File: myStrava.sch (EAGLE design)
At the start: 53 parts, among them Y1 16MHz

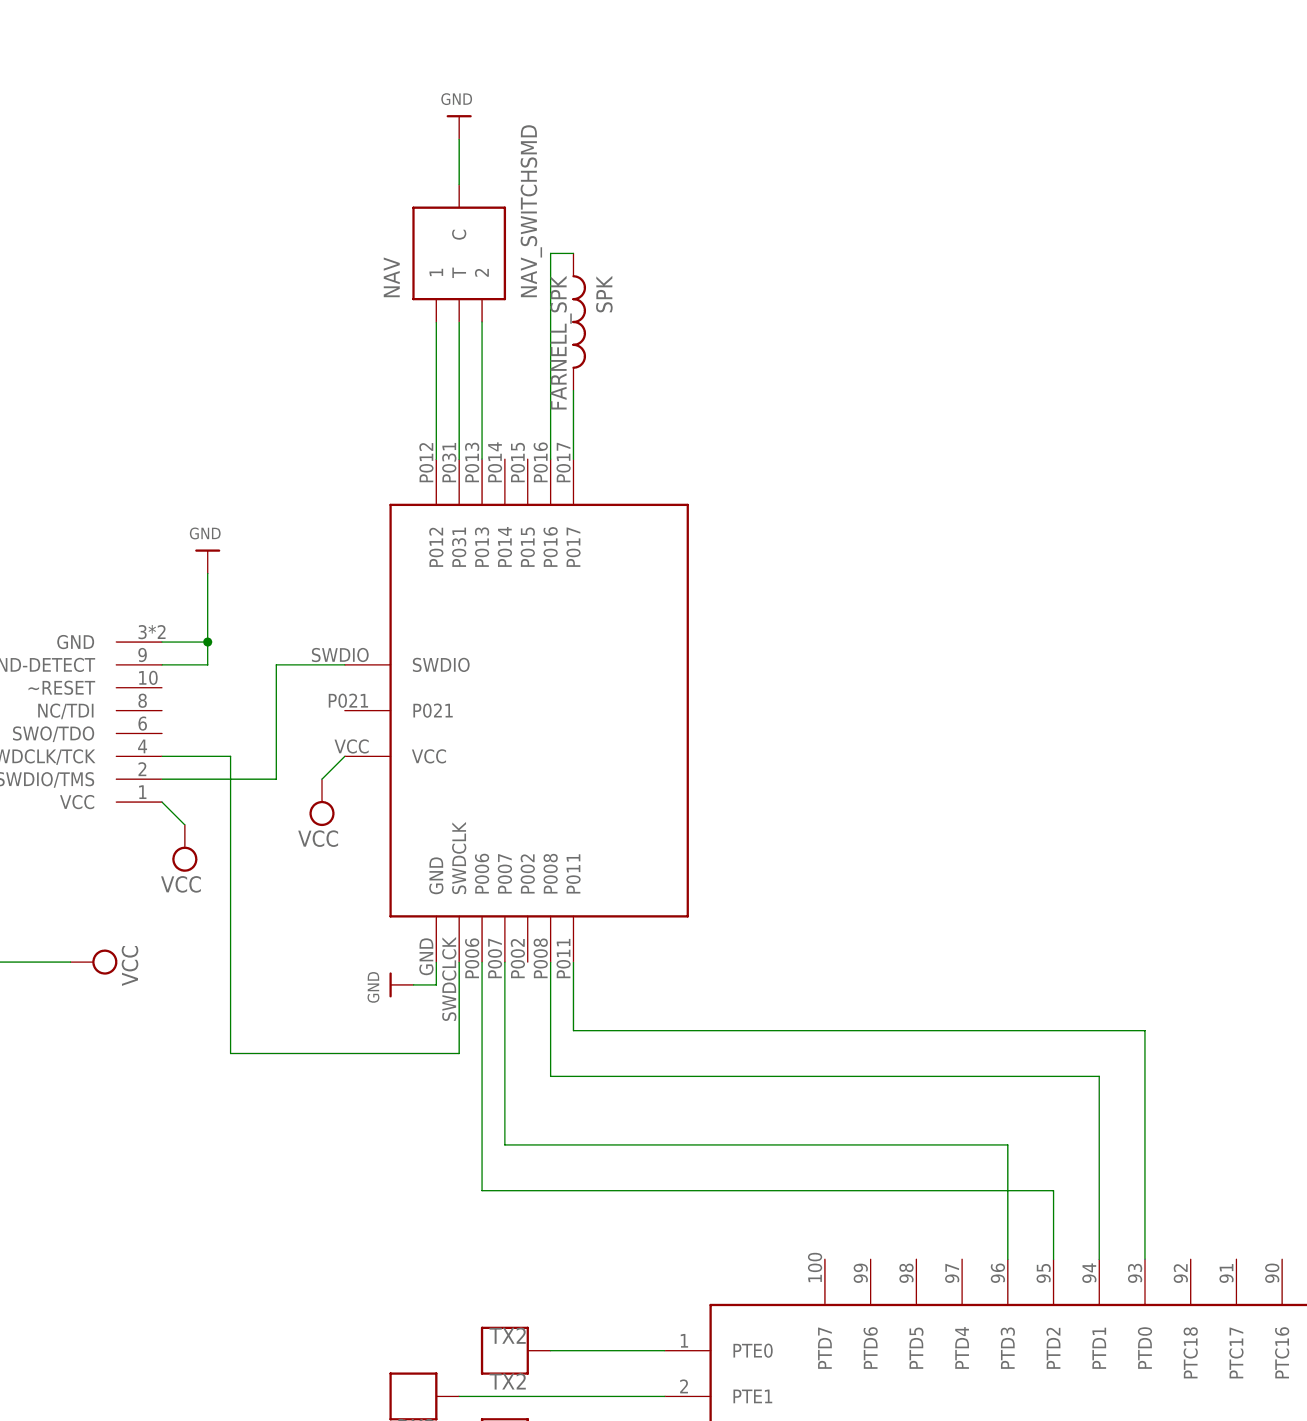
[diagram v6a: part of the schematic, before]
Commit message: Ajout du M8 en face inferieure
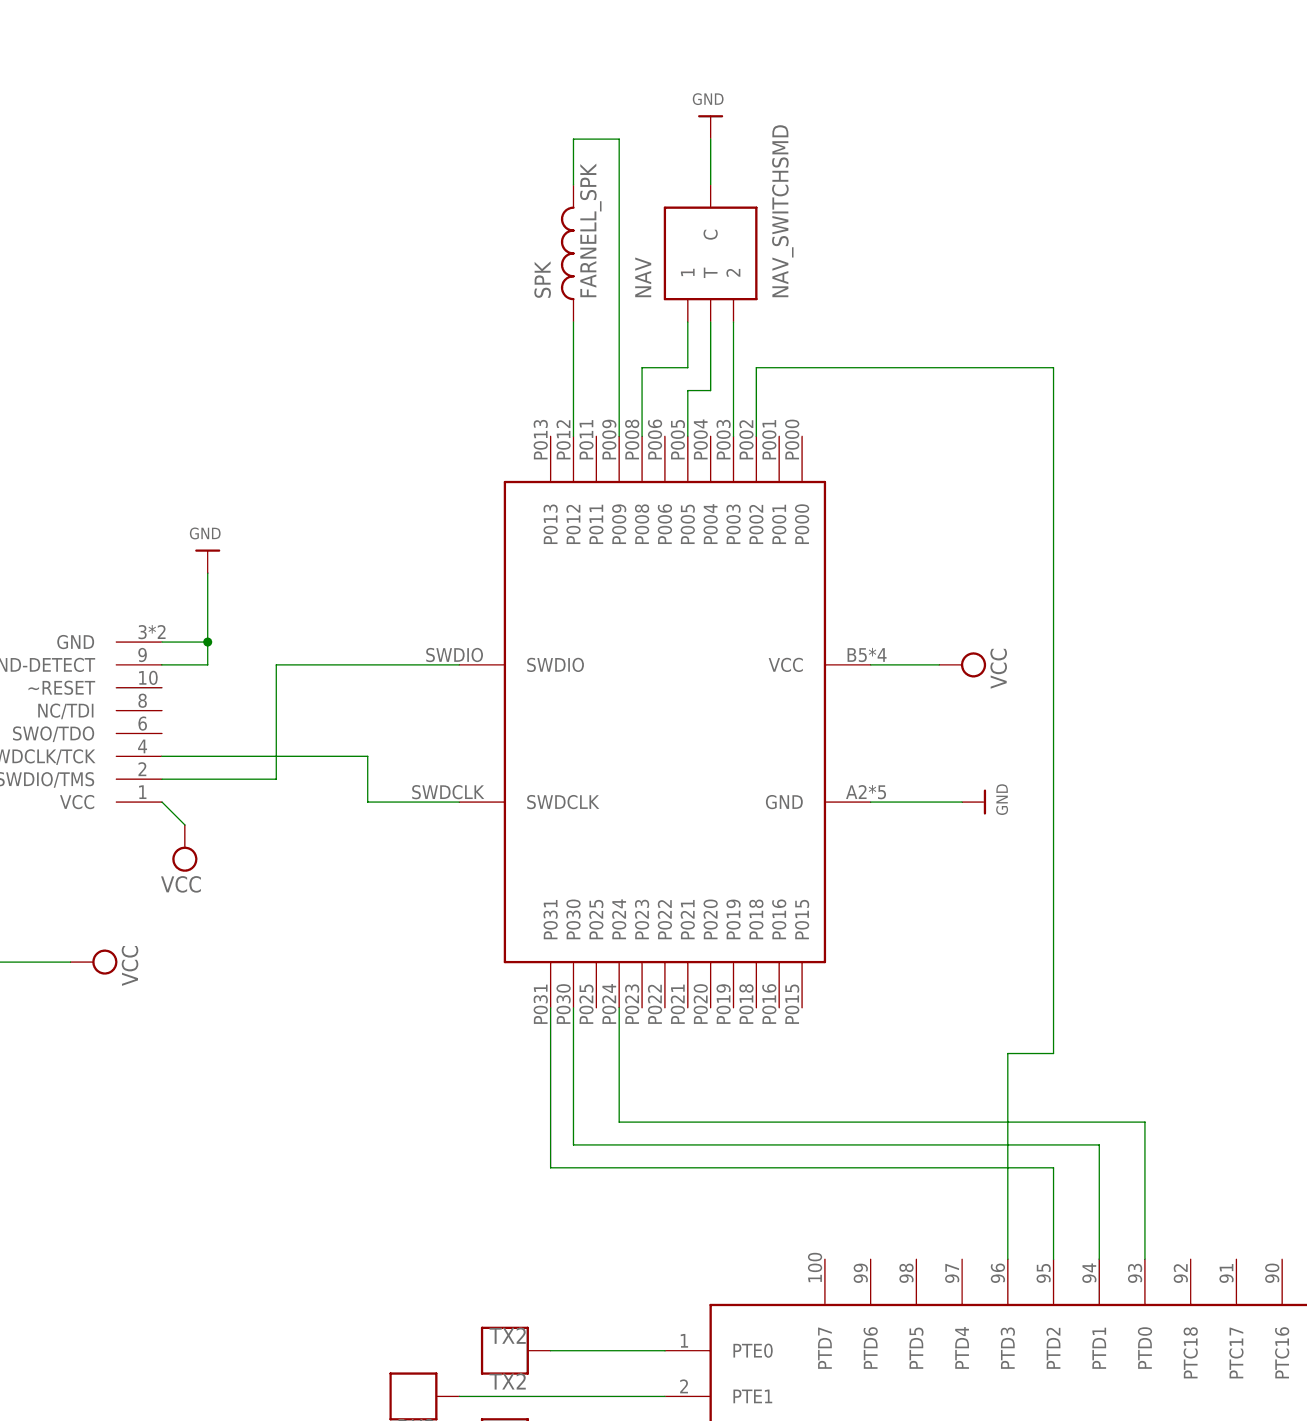
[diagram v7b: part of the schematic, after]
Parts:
- D52Q: value ANTAP28 -> N548; device D52Q:ANTAP28 -> N548:N548
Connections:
- removed net MK_RX3: D52Q.P006, MK20DN512.PTD2
- removed net MK_TX3: D52Q.P007, MK20DN512.PTD3
- new net N$13: D52Q.P024, MK20DN512.PTD0
- new net N$29: D52Q.P002, MK20DN512.PTD3
- net N$10: now also D52Q.P003; no longer D52Q.P013
- net N$18: now also D52Q.P030; no longer D52Q.P008
- net N$21: now also D52Q.P031, MK20DN512.PTD2; no longer D52Q.P011, MK20DN512.PTD0
- net N$3: now also D52Q.P012, SPK.1; no longer D52Q.P017, SPK.2
- net N$7: now also D52Q.P009, SPK.2; no longer D52Q.P016, SPK.1
- net N$8: now also D52Q.P008; no longer D52Q.P012
- net N$9: now also D52Q.P005; no longer D52Q.P031
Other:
- moved on the sheet: NAV, SPK

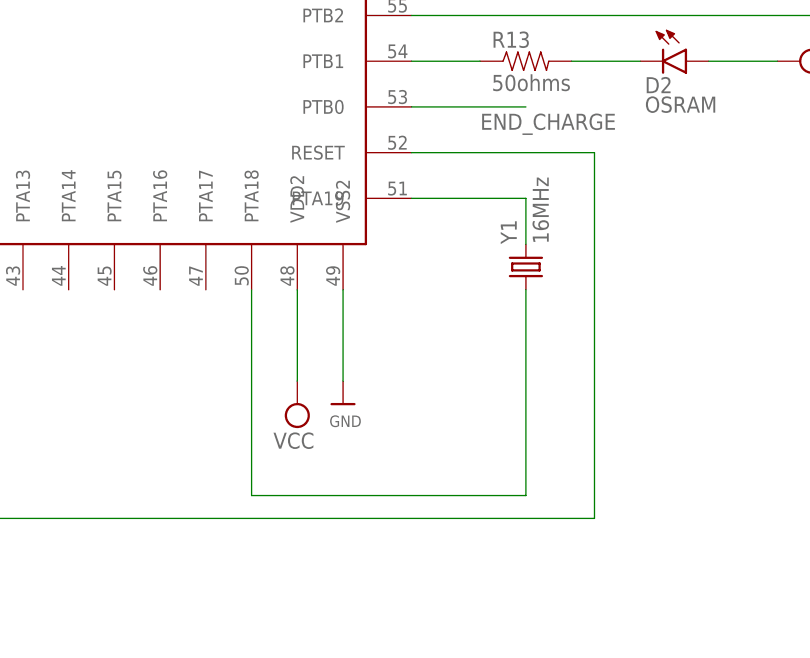
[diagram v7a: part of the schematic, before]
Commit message: Modif d'une via
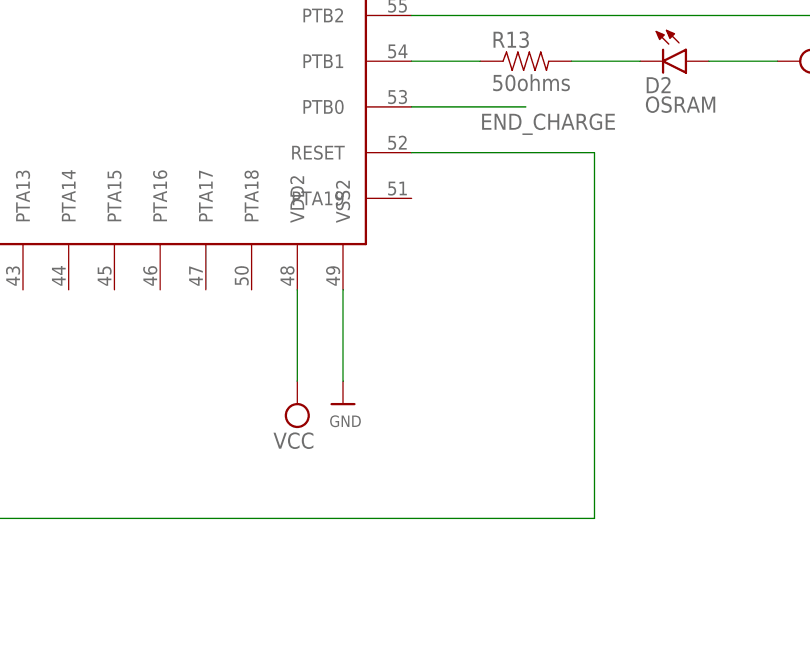
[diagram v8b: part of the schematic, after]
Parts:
- removed Y1: 16MHz, SparkFun-FreqCtrl:CRYSTALHC49UV
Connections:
- removed net N$14: MK20DN512.PTA19, Y1.2
- removed net N$19: MK20DN512.PTA18, Y1.1
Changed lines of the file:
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@@
 <part name="SUPPLY14" library="supply2" deviceset="VCC" device=""/>
 <part name="U$27" library="microbuilder" deviceset="GND" device=""/>
-<part name="Y1" library="SparkFun-FreqCtrl" deviceset="CRYSTAL" device="HC49UV" value="16MHz"/>
 <part name="SUPPLY15" library="supply2" deviceset="VCC" device=""/>
 <part name="C9" library="microbuilder" deviceset="CAP_CERAMIC" device="1206" value="0.1uF"/>
@@
 <instance part="SUPPLY14" gate="G$1" x="33.02" y="-231.14" rot="R180"/>
 <instance part="U$27" gate="G$1" x="38.1" y="-231.14"/>
-<instance part="Y1" gate="G$1" x="58.42" y="-215.9" rot="R90"/>
 <instance part="SUPPLY15" gate="G$1" x="-63.5" y="-236.22" rot="R180"/>
 <instance part="C9" gate="G$1" x="-58.42" y="-236.22"/>
@@
 </segment>
 </net>
-<net name="N$14" class="0">
-<segment>
-<pinref part="Y1" gate="G$1" pin="2"/>
-<wire x1="58.42" y1="-213.36" x2="58.42" y2="-208.28" width="0.1524" layer="91"/>
-<pinref part="MK20DN512" gate="G$1" pin="PTA19"/>
-<wire x1="58.42" y1="-208.28" x2="45.72" y2="-208.28" width="0.1524" layer="91"/>
-</segment>
-</net>
-<net name="N$19" class="0">
-<segment>
-<pinref part="MK20DN512" gate="G$1" pin="PTA18"/>
-<wire x1="27.94" y1="-218.44" x2="27.94" y2="-241.3" width="0.1524" layer="91"/>
-<wire x1="27.94" y1="-241.3" x2="58.42" y2="-241.3" width="0.1524" layer="91"/>
-<pinref part="Y1" gate="G$1" pin="1"/>
-<wire x1="58.42" y1="-241.3" x2="58.42" y2="-218.44" width="0.1524" layer="91"/>
-</segment>
-</net>
